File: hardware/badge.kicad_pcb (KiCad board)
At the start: 2 copper layers, 88 x 156.6 mm, 122 parts, among them J1 Micro_SD_Card, J2 batt, J3 Conn_01x40, J4 USB_C_Receptacle_USB2.0_14P, Q1 AO3400A, Q3 AO3400A, SW1 SW_Push, SW10 SW_Push, SW11 SW_Push, SW12 SW_Push, SW13 SW_Push, SW14 SW_Push, SW15 SW_Push, SW17 SW_Push, SW18 SW_Push, SW19 SW_Push, SW2 SW_Push, SW20 SW_Push, SW21 SW_Push, SW22 SW_Push, SW23 SW_Push, SW25 SW_Push, SW26 SW_Push, SW27 SW_Push, SW28 SW_Push, SW29 SW_Push, SW3 SW_Push, SW30 SW_Push, SW31 SW_Push, SW33 SW_Push, SW34 SW_Push, SW35 SW_Push, SW36 SW_Push, SW37 SW_Push, SW38 SW_Push, SW39 SW_Push, SW4 SW_Push, SW5 SW_Push, SW57 MK-12C02-G020, SW58 SKRHABE010, SW6 SW_Push, SW7 SW_Push, SW8 BOOT, SW9 SW_Push, U1 ESP32-S3-WROOM-1, U10 PCA9555PW, U2 74HC138, U3 BQ24075RGT, U4 TLV62569DBV, U5 BME280, U6 USBLC6-2P6, U7 BMI270, U8 Ai-Thinker-Ra-02, U9 MAX98357A

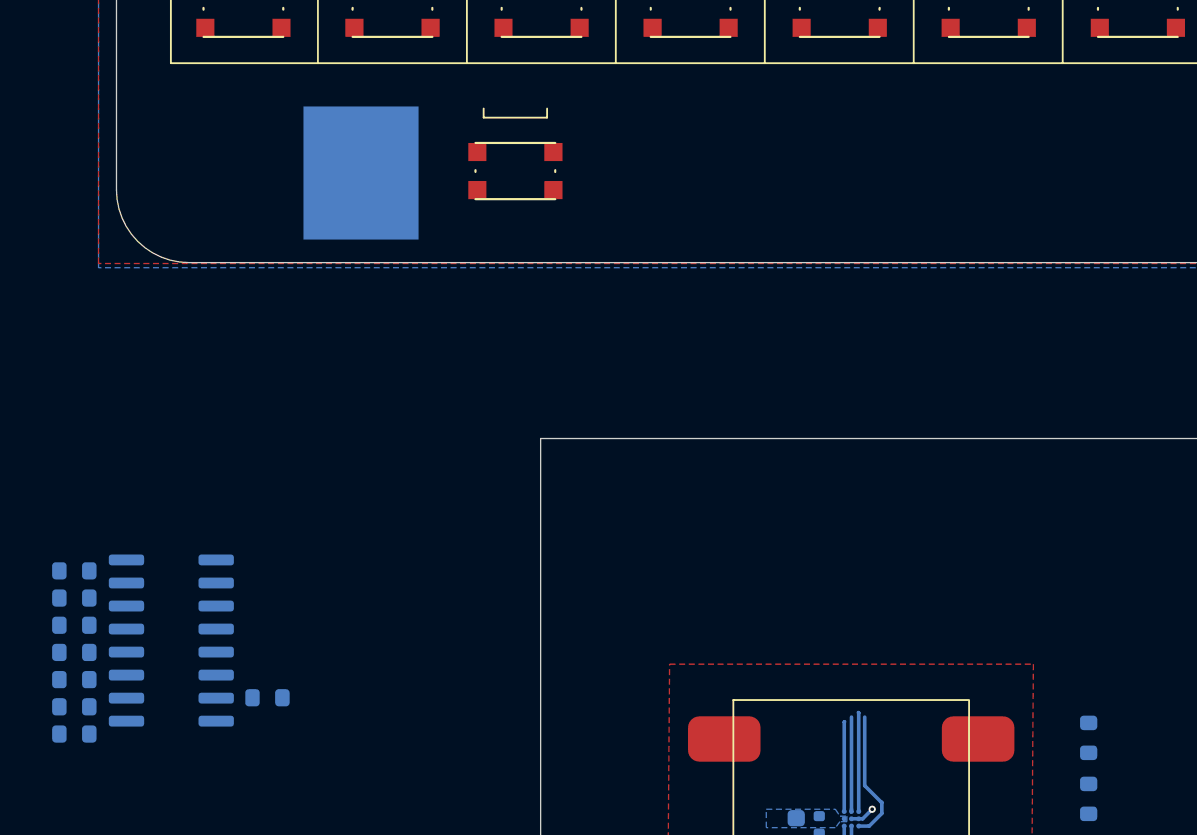
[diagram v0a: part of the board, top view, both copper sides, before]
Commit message: remove mux, use i2c expander for keyboard
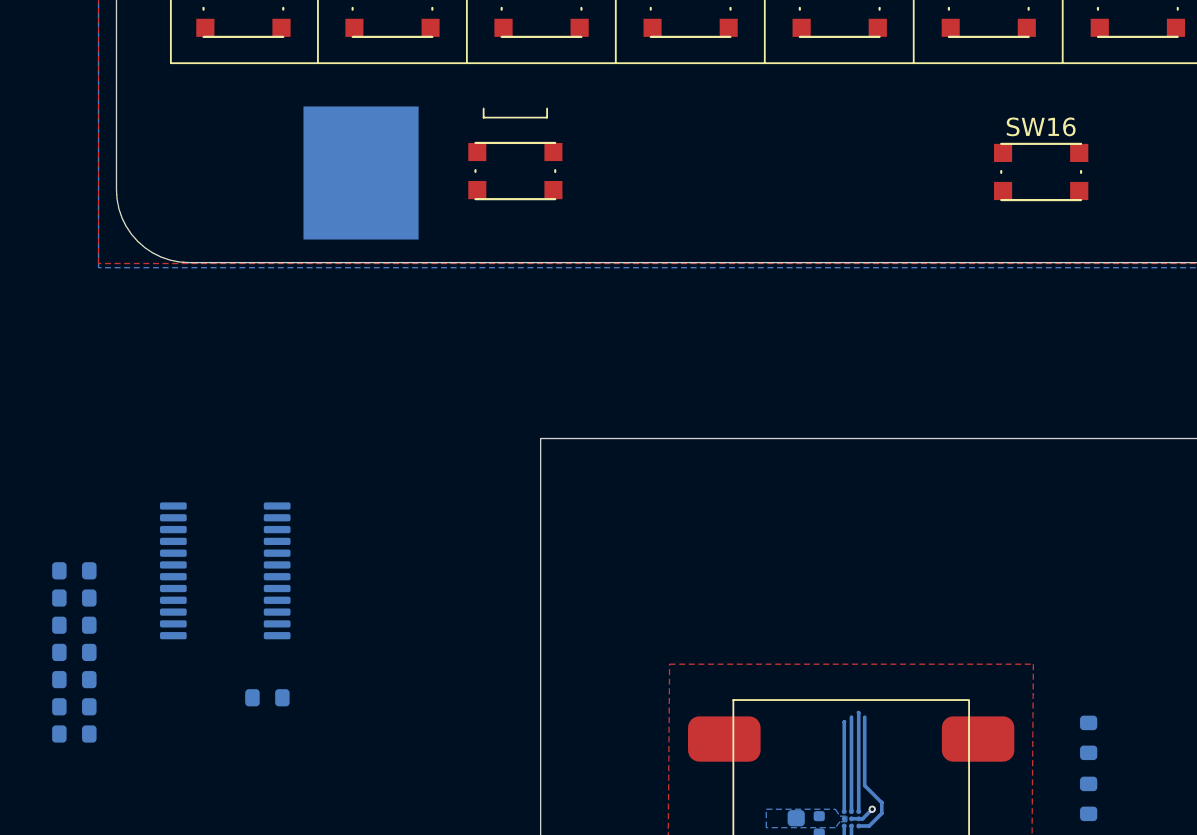
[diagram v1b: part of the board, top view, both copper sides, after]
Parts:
- removed U2: 74HC138, Package_SO:SOIC-16_3.9x9.9mm_P1.27mm
- added SW16: SW_Push, lib:bottonepiccolo_C2888430, F.Cu at (132.0, 141.0)
- added U11: PCA9555PW, Package_SO:TSSOP-24_4.4x7.8mm_P0.65mm, B.Cu at (87.0, 163.0)
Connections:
- SW1 pad 2: /keyboard/KB_COL0 -> Net-(U11-IO0_7)
- SW10 pad 2: /keyboard/KB_COL1 -> Net-(U11-IO0_6)
- SW11 pad 2: /keyboard/KB_COL1 -> Net-(U11-IO0_6)
- SW12 pad 2: /keyboard/KB_COL1 -> Net-(U11-IO0_6)
- SW13 pad 2: /keyboard/KB_COL1 -> Net-(U11-IO0_6)
- SW14 pad 2: /keyboard/KB_COL1 -> Net-(U11-IO0_6)
- SW15 pad 2: /keyboard/KB_COL1 -> Net-(U11-IO0_6)
- SW17 pad 2: /keyboard/KB_COL2 -> Net-(U11-IO0_5)
- SW18 pad 2: /keyboard/KB_COL2 -> Net-(U11-IO0_5)
- SW19 pad 2: /keyboard/KB_COL2 -> Net-(U11-IO0_5)
- SW2 pad 2: /keyboard/KB_COL0 -> Net-(U11-IO0_7)
- SW20 pad 2: /keyboard/KB_COL2 -> Net-(U11-IO0_5)
- SW21 pad 2: /keyboard/KB_COL2 -> Net-(U11-IO0_5)
- SW22 pad 2: /keyboard/KB_COL2 -> Net-(U11-IO0_5)
- SW23 pad 2: /keyboard/KB_COL2 -> Net-(U11-IO0_5)
- SW25 pad 2: /keyboard/KB_COL3 -> Net-(U11-IO0_4)
- SW26 pad 2: /keyboard/KB_COL3 -> Net-(U11-IO0_4)
- SW27 pad 2: /keyboard/KB_COL3 -> Net-(U11-IO0_4)
- SW28 pad 2: /keyboard/KB_COL3 -> Net-(U11-IO0_4)
- SW29 pad 2: /keyboard/KB_COL3 -> Net-(U11-IO0_4)
- SW3 pad 2: /keyboard/KB_COL0 -> Net-(U11-IO0_7)
- SW30 pad 2: /keyboard/KB_COL3 -> Net-(U11-IO0_4)
- SW31 pad 2: /keyboard/KB_COL3 -> Net-(U11-IO0_4)
- SW33 pad 2: /keyboard/KB_COL4 -> Net-(U11-IO0_3)
- SW34 pad 2: /keyboard/KB_COL4 -> Net-(U11-IO0_3)
- SW35 pad 2: /keyboard/KB_COL4 -> Net-(U11-IO0_3)
- SW36 pad 2: /keyboard/KB_COL4 -> Net-(U11-IO0_3)
- SW37 pad 2: /keyboard/KB_COL4 -> Net-(U11-IO0_3)
- SW38 pad 2: /keyboard/KB_COL4 -> Net-(U11-IO0_3)
- SW39 pad 2: /keyboard/KB_COL4 -> Net-(U11-IO0_3)
- SW4 pad 2: /keyboard/KB_COL0 -> Net-(U11-IO0_7)
- SW5 pad 2: /keyboard/KB_COL0 -> Net-(U11-IO0_7)
- SW58 pad 1: /keyboard/KB_COL2 -> Net-(U11-IO0_5)
- SW58 pad 2: /keyboard/KB_COL3 -> Net-(U11-IO0_4)
- SW58 pad 3: /keyboard/KB_COL4 -> Net-(U11-IO0_3)
- SW58 pad 4: /keyboard/KB_COL1 -> Net-(U11-IO0_6)
- SW58 pad 6: /keyboard/KB_COL0 -> Net-(U11-IO0_7)
- SW6 pad 2: /keyboard/KB_COL0 -> Net-(U11-IO0_7)
- SW7 pad 2: /keyboard/KB_COL0 -> Net-(U11-IO0_7)
- SW9 pad 2: /keyboard/KB_COL1 -> Net-(U11-IO0_6)
- U10 pad 13: /keyboard/KB_COL4 -> unconnected-(U10-IO1_0-Pad13)
- U10 pad 14: /keyboard/KB_COL3 -> unconnected-(U10-IO1_1-Pad14)
- U10 pad 15: /keyboard/KB_COL2 -> unconnected-(U10-IO1_2-Pad15)
- U10 pad 16: /keyboard/KB_COL1 -> unconnected-(U10-IO1_3-Pad16)
- U10 pad 17: /keyboard/KB_COL0 -> unconnected-(U10-IO1_4-Pad17)
- U10 pad 18: /keyboard/KB_ROW2 -> unconnected-(U10-IO1_5-Pad18)
- U10 pad 19: /keyboard/KB_ROW1 -> unconnected-(U10-IO1_6-Pad19)
- U10 pad 20: /keyboard/KB_ROW0 -> unconnected-(U10-IO1_7-Pad20)

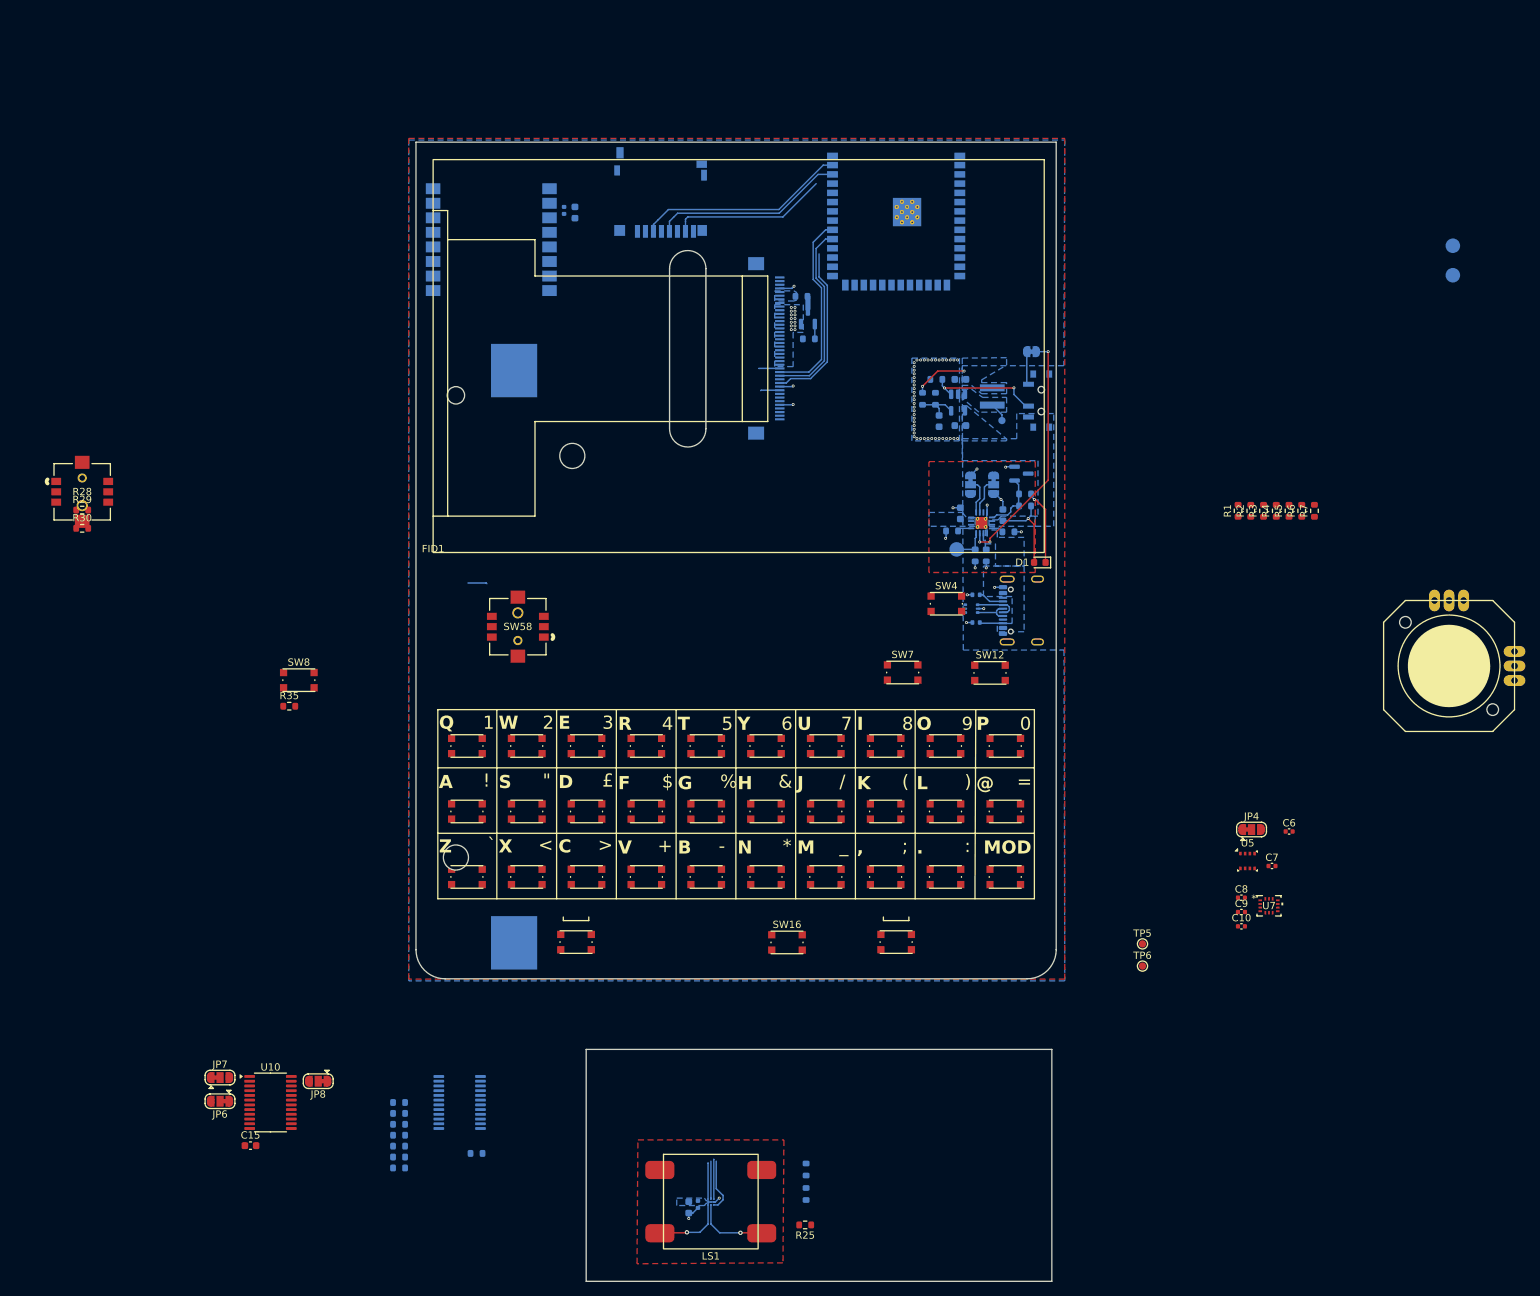
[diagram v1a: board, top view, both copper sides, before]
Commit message: reorganize keyboard buttons for layout
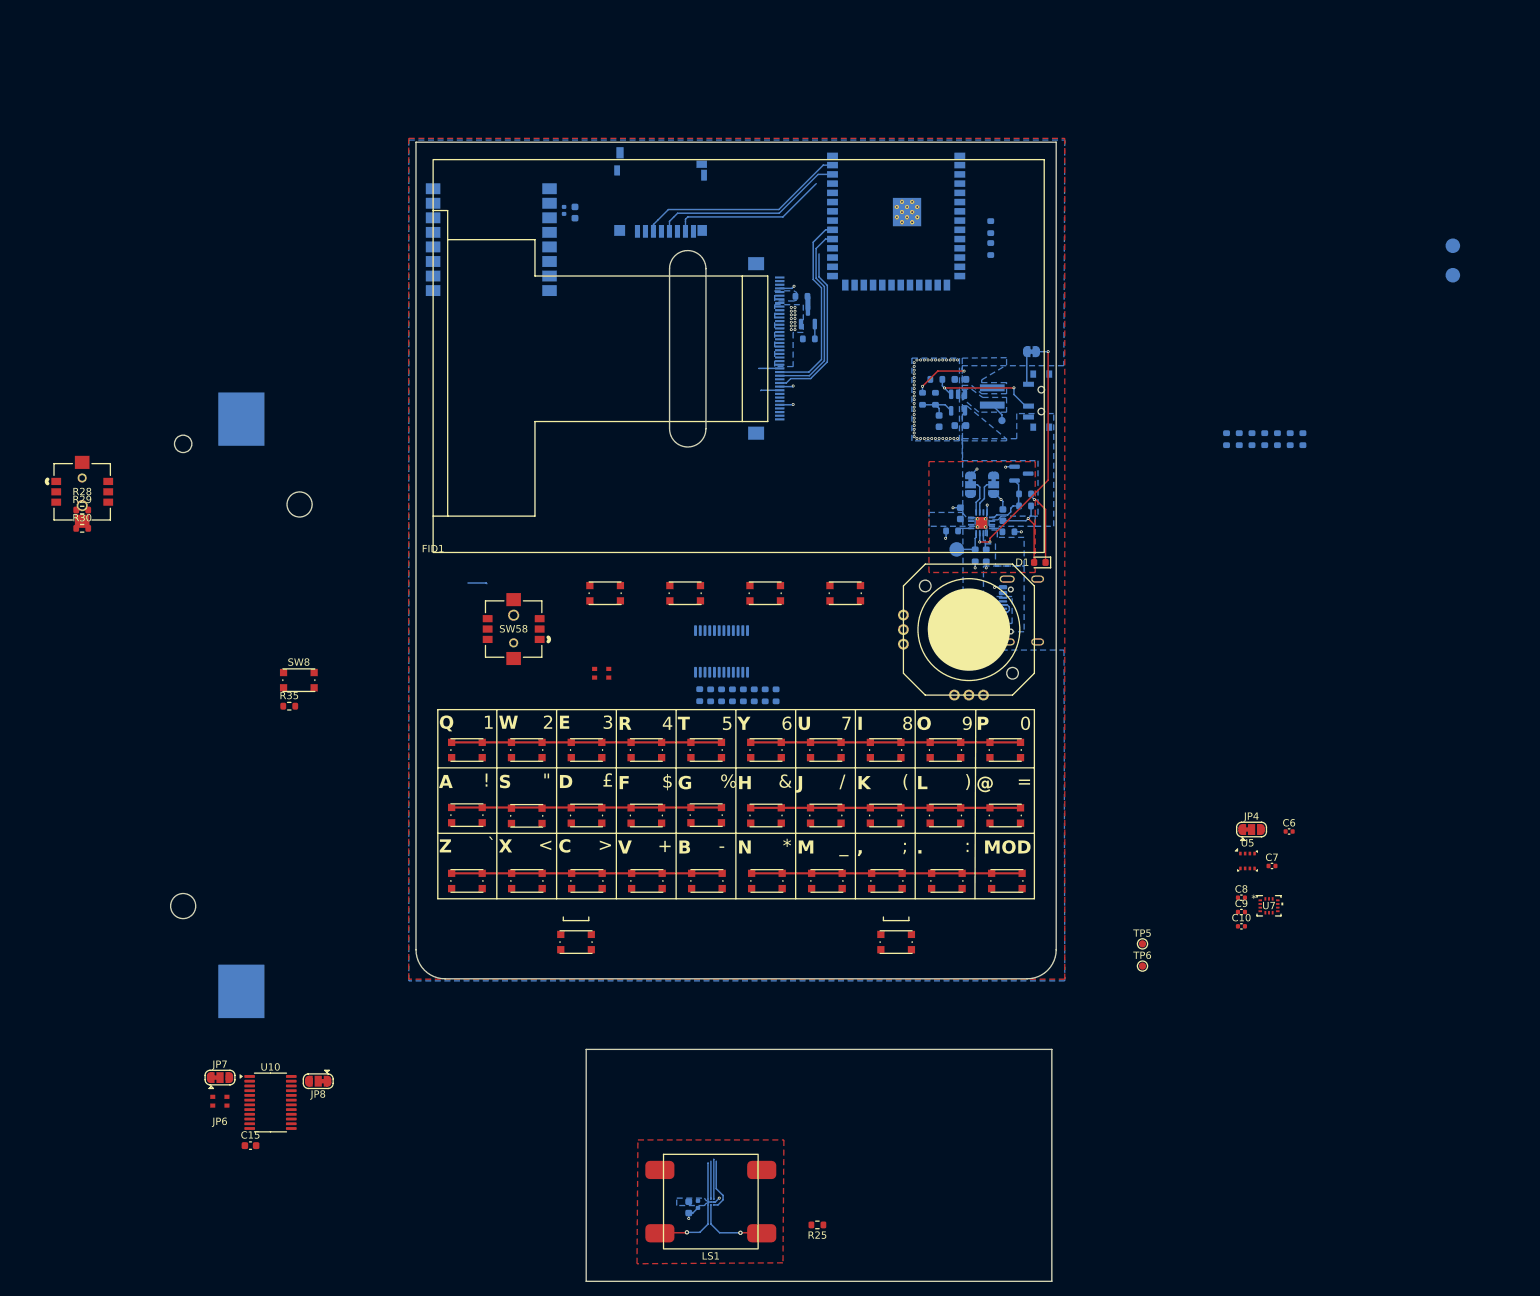
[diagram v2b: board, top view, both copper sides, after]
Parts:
- added MK1: Microphone_Crystal, lib:microfono, F.Cu at (106.5, 104.0)
- JP6: footprint Jumper:SolderJumper-3_P1.3mm_Bridged12_RoundedPad1.0x1.5mm -> lib:microfono
- R1, R2, R3, R4, R5, R6, R7: moved to B.Cu
- moved R33 135.3 mm to (160.0, 42.7), turned to 90 degrees
- moved R34 129.0 mm to (160.0, 45.7), turned to 90 degrees
- moved R14 77.8 mm to (121.5, 107.0), turned to -90 degrees
- moved R13 77.4 mm to (123.0, 107.0), turned to -90 degrees
- moved R12 77.1 mm to (124.5, 107.0), turned to -90 degrees
- moved R11 76.8 mm to (126.0, 107.0), turned to -90 degrees
- moved R10 76.6 mm to (127.5, 107.0), turned to -90 degrees
- moved R9 76.4 mm to (129.0, 107.0), turned to -90 degrees
- moved R8 76.3 mm to (130.5, 107.0), turned to -90 degrees
- moved U11 71.7 mm to (123.0, 101.0), turned to -90 degrees
- moved R15 70.1 mm to (120.0, 107.0), turned to -90 degrees
- moved SW4 68.9 mm to (88.0, 114.5)
- moved RV1 66.2 mm to (157.0, 98.0), turned to 180 degrees
- moved SW12 64.6 mm to (96.2, 114.5)
- moved SW5 58.3 mm to (88.0, 123.5)
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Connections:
- U1 pad 7: unconnected-(U1-IO7-Pad7) -> /mcu/MICROPHONE
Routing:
- net Net-(R8-Pad2): track 0.00 -> 37.2 mm
- net Net-(R13-Pad2): track 0.00 -> 37.2 mm
- net Net-(R9-Pad2): track 0.00 -> 37.1 mm
- net Net-(R10-Pad2): track 0.00 -> 37.1 mm
- net Net-(R12-Pad2): track 0.00 -> 37.1 mm
- net Net-(R11-Pad2): track 0.00 -> 37.1 mm

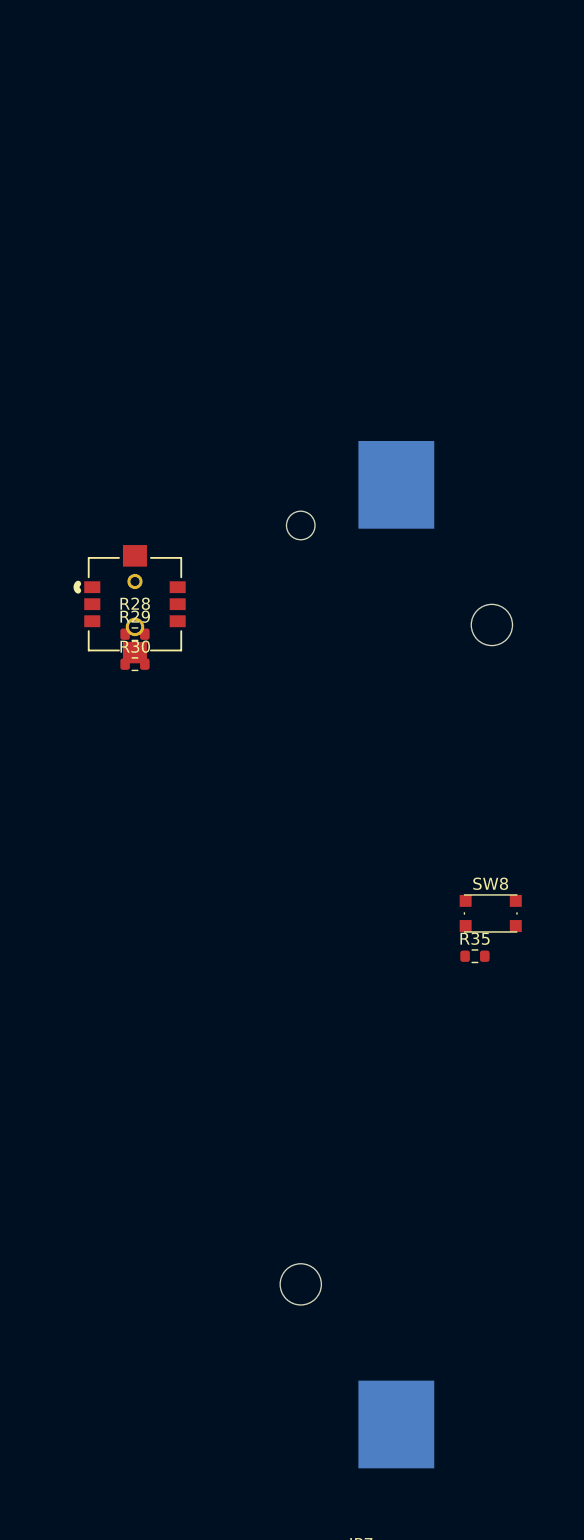
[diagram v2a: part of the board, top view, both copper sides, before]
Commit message: Add MY-18650-01 footprint and 3d model
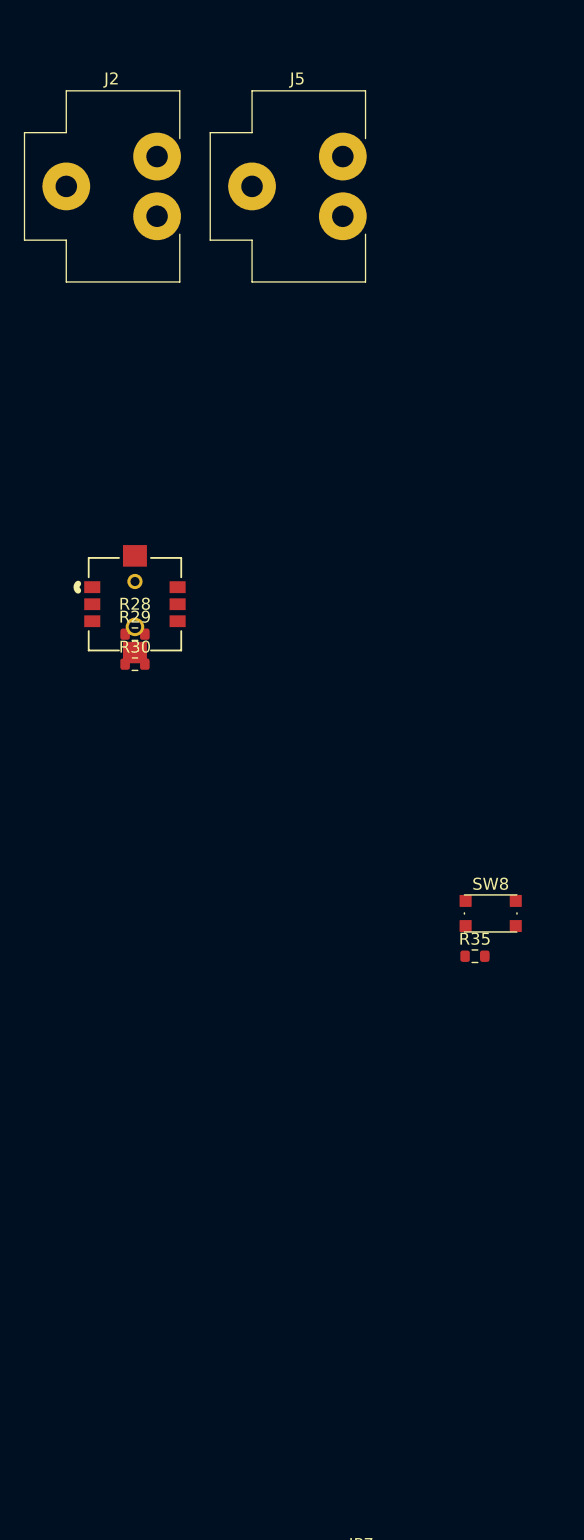
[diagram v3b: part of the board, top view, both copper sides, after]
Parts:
- added J5: MY-18650-01, lib:MY-18650-01, F.Cu at (48.7, 44.1)
- J2: value batt -> MY-18650-01; footprint Battery:BatteryHolder_Keystone_1042_1x18650 -> lib:MY-18650-01; moved to F.Cu
- moved J2 68.6 mm to (33.2, 44.1), turned to 0 degrees
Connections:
- C3 pad 1: Net-(J2-Pin_2) -> Net-(J5-Pin_1)
- U3 pad 2: Net-(J2-Pin_2) -> Net-(J5-Pin_1)
- U3 pad 3: Net-(J2-Pin_2) -> Net-(J5-Pin_1)
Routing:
- added copper zone on B.Cu, net Net-(J5-Pin_1)
- removed copper zone on B.Cu, net Net-(J2-Pin_2)
